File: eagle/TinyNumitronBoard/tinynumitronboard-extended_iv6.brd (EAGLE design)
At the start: 100 x 50 mm, 42 parts

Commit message: Last changes but problem with drill holes
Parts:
- removed U$3: (no value), kalshagar-images:GEARS_1000X500
- added U$1: (no value), kalshagar-images:SNOW1_1000X500
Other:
- board text added: "DATA (in)"
- board text added: "DATA (out)"
- board text removed: "DATA(in)"
- board text removed: "DATA(out)"
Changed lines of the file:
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@@
 <layer number="207" name="207bmp" color="8" fill="10" visible="no" active="yes"/>
 <layer number="208" name="208bmp" color="9" fill="10" visible="no" active="yes"/>
-<layer number="209" name="209bmp" color="7" fill="1" visible="no" active="yes"/>
+<layer number="209" name="209bmp" color="7" fill="1" visible="yes" active="yes"/>
 <layer number="210" name="210bmp" color="7" fill="1" visible="no" active="yes"/>
 <layer number="211" name="211bmp" color="7" fill="1" visible="no" active="yes"/>
@@
 <text x="8.89" y="19.685" size="1.27" layer="52" font="vector" rot="MR0">LTCH</text>
 <text x="96.2025" y="19.685" size="1.27" layer="52" font="vector" rot="MR0">LTCH</text>
-<text x="12.065" y="24.765" size="1.27" layer="52" font="vector" rot="MR0">DATA(in)</text>
+<text x="8.493125" y="22.780625" size="1.27" layer="52" font="vector" rot="MR0">DATA
+(in)</text>
 <wire x1="1.27" y1="21.59" x2="3.81" y2="21.59" width="0.4064" layer="52"/>
 <wire x1="3.81" y1="21.59" x2="3.81" y2="26.67" width="0.4064" layer="52"/>
@@
 <wire x1="99.06" y1="21.59" x2="96.52" y2="21.59" width="0.4064" layer="52"/>
 <wire x1="96.52" y1="21.59" x2="96.52" y2="26.67" width="0.4064" layer="52"/>
-<text x="95.885" y="24.765" size="1.27" layer="52" font="vector" rot="MR0">DATA(out)</text>
+<text x="96.123125" y="23.1775" size="1.27" layer="52" font="vector" rot="MR0">DATA
+(out)</text>
 <text x="76.2" y="48.26" size="1.27" layer="52" font="vector" rot="MR0">http://electrogeek.cc/Alan numitron clock.html</text>
-<wire x1="76.2" y1="30.48" x2="72.39" y2="36.83" width="0.6096" layer="52"/>
-<wire x1="72.39" y1="36.83" x2="72.39" y2="30.48" width="0.6096" layer="52"/>
-<wire x1="72.39" y1="30.48" x2="72.39" y2="24.13" width="0.6096" layer="52"/>
-<wire x1="72.39" y1="24.13" x2="68.58" y2="30.48" width="0.6096" layer="52"/>
-<wire x1="72.39" y1="30.48" x2="74.93" y2="30.48" width="0.6096" layer="52"/>
+<wire x1="78.74" y1="27.94" x2="74.93" y2="34.29" width="0.6096" layer="52"/>
+<wire x1="74.93" y1="34.29" x2="74.93" y2="29.21" width="0.6096" layer="52"/>
+<wire x1="74.93" y1="29.21" x2="74.93" y2="22.86" width="0.6096" layer="52"/>
+<wire x1="74.93" y1="22.86" x2="71.12" y2="29.21" width="0.6096" layer="52"/>
+<wire x1="74.93" y1="29.21" x2="77.47" y2="29.21" width="0.6096" layer="52"/>
 <text x="70.1675" y="0.635" size="1.27" layer="52" font="vector" rot="MR0">Alan numitron clock - IV6 (v1.0 - Dec 2016)</text>
 <text x="0.635" y="28.575" size="1.4224" layer="52" font="vector" rot="MR180">[IN]</text>
@@
 <element name="H2" library="holes" package="2,8" value="MOUNT-HOLE2.8" x="96.52" y="46.0375"/>
 <element name="H3" library="holes" package="2,8" value="MOUNT-HOLE2.8" x="96.52" y="3.81" locked="yes"/>
-<element name="U$3" library="kalshagar-images" package="GEARS_1000X500" value="" x="1.5875" y="0.635"/>
 <element name="TUBE1" library="kalshagar" package="IV6_NUMITRON_PAC_LARGE" value="IV6_NUMITRONLARGE" x="15" y="25"/>
 <element name="DRIVER1" library="uln2803" package="SO18L" value="ULN2803" x="15.24" y="39.37" rot="MR180"/>
@@
 <element name="JP_DOT_TUBE1" library="SparkFun-Passives" package="PAD-JUMPER-2-NO_YES_SILK" value="JUMPER-PAD-2-NOYES_SILK" x="24.13" y="29.21" rot="MR270"/>
 <element name="JP_DOT_TUBE4" library="SparkFun-Passives" package="PAD-JUMPER-2-NO_YES_SILK" value="JUMPER-PAD-2-NOYES_SILK" x="76.2" y="16.51" rot="MR90"/>
+<element name="U$1" library="kalshagar-images" package="SNOW1_1000X500" value="" x="0" y="0"/>
 </elements>
 <signals>

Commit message: Crapped up, now fixing
Started version 2, ripped up everything
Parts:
- removed DRIVER2: ULN2803, uln2803:SO18L
- removed TP1, TP2, TP3, TP4: TPB2,54, testpad:B2,54
- added IC1: IC_TD62783-SO-18W, dp_devices:SO-18L
- JP_INPUT, JP_OUTPUT: device SparkFun:1X06 -> SparkFun-Connectors:1X05_NO_SILK
- moved JP_INPUT 2.54 mm to (2.54, 15.2)
- moved JP_OUTPUT 2.54 mm to (97.8, 15.2)
- moved J_LED_IN 2.54 mm to (2.54, 12.7)
- moved J_LED_OUT 2.54 mm to (97.8, 12.7)
- moved J_TUBEPOWER_IN 2.54 mm to (2.54, 27.9)
- moved J_TUBEPOWER_OUT 2.54 mm to (97.8, 27.9)
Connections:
- removed net DIODE: DRIVER1.10, DRIVER2.10, DRIVER3.10, DRIVER4.10, TP1.TP, TP2.TP, TP3.TP, TP4.TP
- net GND: now also IC1.9; no longer DRIVER2.9
- net GRID_P: now also IC1.10
- net N$14: now also IC1.17; no longer DRIVER2.18
- net N$16: now also IC1.18; no longer DRIVER2.17
- net N$17: now also IC1.16; no longer DRIVER2.16
- net N$21: no longer JP_OUTPUT.6
- net N$39: now also IC1.15; no longer DRIVER2.15
- net N$40: now also IC1.14; no longer DRIVER2.14
- net N$41: now also IC1.13; no longer DRIVER2.13
- net N$42: now also IC1.12; no longer DRIVER2.12
- net N$43: now also IC1.11; no longer DRIVER2.11
- net N$44: now also IC1.1; no longer DRIVER2.1
- net N$45: now also IC1.2; no longer DRIVER2.2
- net N$46: now also IC1.3; no longer DRIVER2.3
- net N$47: now also IC1.4; no longer DRIVER2.4
- net N$48: now also IC1.5; no longer DRIVER2.5
- net N$49: now also IC1.6; no longer DRIVER2.6
- net N$50: now also IC1.7; no longer DRIVER2.7
- net N$51: now also IC1.8; no longer DRIVER2.8
- net SER: no longer JP_INPUT.6
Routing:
- net VCC: track 258.2 -> 0.00 mm, vias 5 -> 0
- net FIL_M: track 204.9 -> 0.00 mm
- net RCK: track 202.9 -> 0.00 mm, vias 4 -> 0
- net SCK: track 188.5 -> 0.00 mm, vias 6 -> 0
- net N$13: track 154.2 -> 0.00 mm, vias 2 -> 0
- net FIL_P: track 133.1 -> 0.00 mm
- net GRID_P: track 117.2 -> 0.00 mm, vias 3 -> 0
- net N$23: track 47.9 -> 0.00 mm, vias 2 -> 0
- net N$21: track 46.2 -> 0.00 mm, vias 1 -> 0
- net N$65: track 39.8 -> 0.00 mm
- net N$53: track 39.8 -> 0.00 mm, vias 2 -> 0
- net SER: track 38.5 -> 0.00 mm, vias 1 -> 0
- net N$10: track 36.4 -> 0.00 mm, vias 2 -> 0
- net N$32: track 31.3 -> 0.00 mm
- net N$30: track 30.4 -> 0.00 mm
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- removed copper zone on layer 16, net GND
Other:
- board text added: "Alan numitron clock - IV6 (v2.0 - Jan 2017)"
- board text added: "DATA"
- board text added: "TD62783"
- board text added: "http://electrogeek.cc/Alan numitron clock iv6.html"
- board text removed: "Alan numitron clock - IV6 (v1.0 - Dec 2016)"
- board text removed: "DATA (in)"
- board text removed: "DATA (out)"
- board text removed: "http://electrogeek.cc/Alan numitron clock.html"

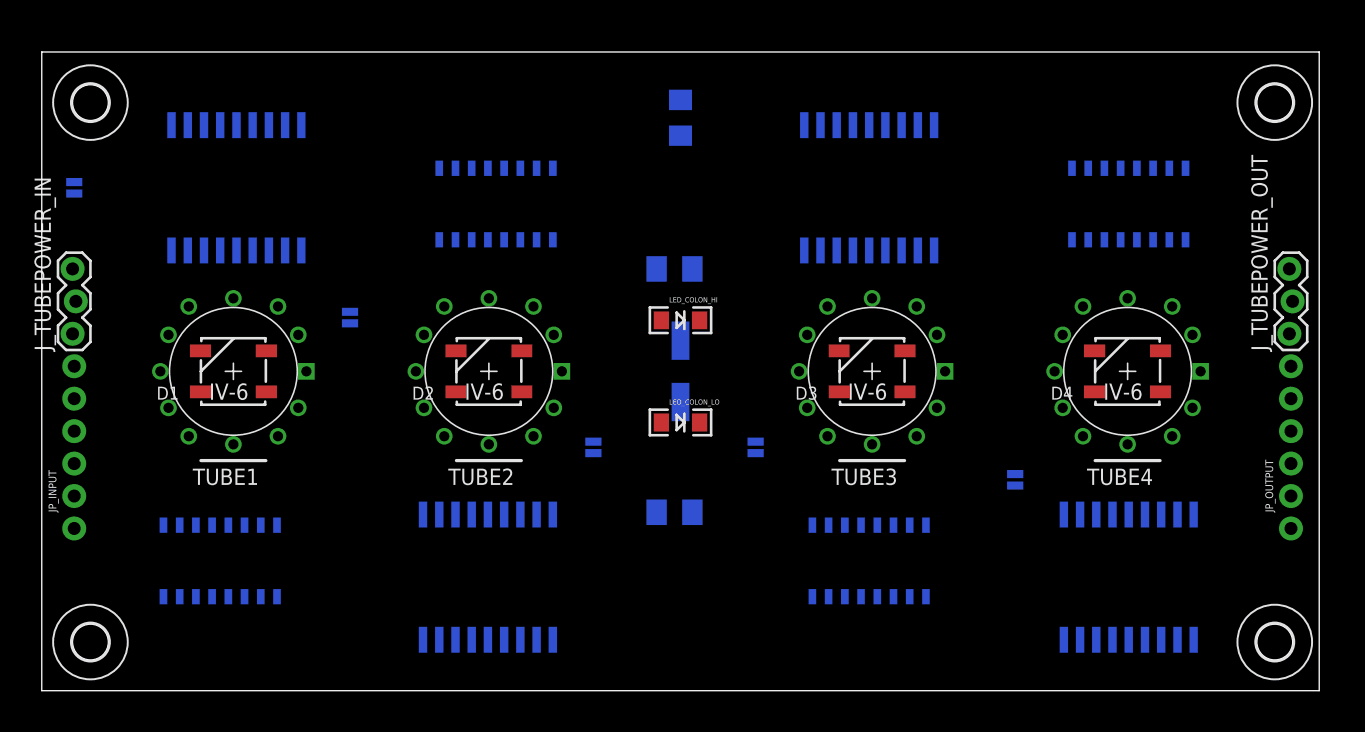
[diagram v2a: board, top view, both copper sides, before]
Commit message: Schematic fixed, placement done
Need to do routing now
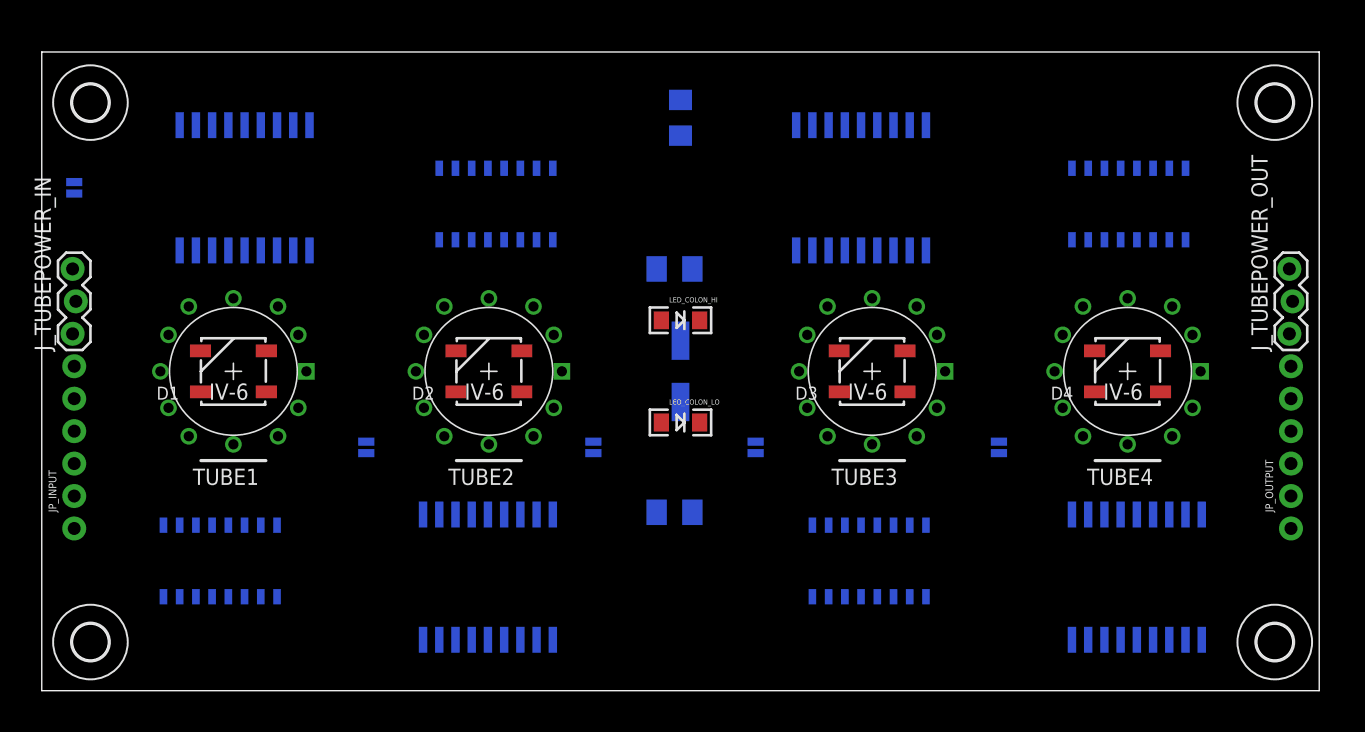
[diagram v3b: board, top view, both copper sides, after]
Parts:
- removed DRIVER1, DRIVER3, DRIVER4: ULN2803, uln2803:SO18L
- added PNPARRAY1, PNPARRAY3, PNPARRAY4: IC_TD62783-SO-18W, dp_devices:SO-18L
- moved JP_DOT_TUBE1 10.2 mm to (25.4, 19.1)
- moved JP_DOT_TUBE4 2.84 mm to (74.9, 19.1)
- renumbered IC1 to PNPARRAY2
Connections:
- net GND: now also PNPARRAY1.9, PNPARRAY3.9, PNPARRAY4.9; no longer DRIVER1.9, DRIVER3.9, DRIVER4.9
- net GRID_P: now also PNPARRAY1.10, PNPARRAY3.10, PNPARRAY4.10
- net N$1: now also PNPARRAY1.5, SER1.4; no longer DRIVER1.1, SER1.15
- net N$14: now also PNPARRAY2.18; no longer PNPARRAY2.17
- net N$15: now also PNPARRAY1.18; no longer DRIVER1.18
- net N$16: now also PNPARRAY2.17; no longer PNPARRAY2.18
- net N$18: now also PNPARRAY1.17; no longer DRIVER1.17
- net N$19: now also PNPARRAY1.16; no longer DRIVER1.16
- net N$2: now also PNPARRAY1.4, SER1.3; no longer DRIVER1.2, SER1.1
- net N$24: now also PNPARRAY4.18; no longer DRIVER4.18
- net N$25: now also PNPARRAY4.17; no longer DRIVER4.17
- net N$26: now also PNPARRAY4.16; no longer DRIVER4.16
- net N$27: now also PNPARRAY4.15; no longer DRIVER4.15
- net N$28: now also PNPARRAY4.14; no longer DRIVER4.14
- net N$29: now also PNPARRAY4.13; no longer DRIVER4.13
- net N$3: now also PNPARRAY1.3; no longer DRIVER1.3
- net N$30: now also PNPARRAY4.12; no longer DRIVER4.12
- net N$31: now also PNPARRAY4.11; no longer DRIVER4.11
- net N$32: now also PNPARRAY4.1; no longer DRIVER4.1
- net N$33: now also PNPARRAY4.2; no longer DRIVER4.2
- net N$34: now also PNPARRAY4.3; no longer DRIVER4.3
- net N$35: now also PNPARRAY4.4; no longer DRIVER4.4
- net N$36: now also PNPARRAY4.5; no longer DRIVER4.5
- net N$37: now also PNPARRAY4.6; no longer DRIVER4.6
- net N$38: now also PNPARRAY1.15; no longer DRIVER1.15
- net N$4: now also PNPARRAY1.2, SER1.1; no longer DRIVER1.4, SER1.3
- net N$5: now also PNPARRAY1.1, SER1.15; no longer DRIVER1.5, SER1.4
- net N$52: now also PNPARRAY4.7; no longer DRIVER4.7
- net N$54: now also PNPARRAY3.18; no longer DRIVER3.18
- net N$55: now also PNPARRAY1.14; no longer DRIVER1.14
- net N$56: now also PNPARRAY1.13; no longer DRIVER1.13
- net N$57: now also PNPARRAY1.12; no longer DRIVER1.12
- net N$58: now also PNPARRAY3.17; no longer DRIVER3.17
- net N$59: now also PNPARRAY1.11; no longer DRIVER1.11
- net N$6: now also PNPARRAY1.6; no longer DRIVER1.6
- net N$60: now also PNPARRAY3.16; no longer DRIVER3.16
- net N$61: now also PNPARRAY3.15; no longer DRIVER3.15
- net N$62: now also PNPARRAY3.14; no longer DRIVER3.14
- net N$63: now also PNPARRAY3.13; no longer DRIVER3.13
- net N$64: now also PNPARRAY3.12; no longer DRIVER3.12
- net N$65: now also PNPARRAY3.11; no longer DRIVER3.11
- net N$66: now also PNPARRAY3.1; no longer DRIVER3.1
- net N$67: now also PNPARRAY3.2; no longer DRIVER3.2
- net N$68: now also PNPARRAY3.3; no longer DRIVER3.3
- net N$69: now also PNPARRAY3.4; no longer DRIVER3.4
- net N$7: now also PNPARRAY1.7; no longer DRIVER1.7
- net N$70: now also PNPARRAY3.5; no longer DRIVER3.5
- net N$71: now also PNPARRAY3.6; no longer DRIVER3.6
- net N$72: now also PNPARRAY3.7; no longer DRIVER3.7
- net N$73: now also PNPARRAY3.8; no longer DRIVER3.8
- net N$74: now also PNPARRAY4.8; no longer DRIVER4.8
- net N$8: now also PNPARRAY1.8; no longer DRIVER1.8
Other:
- board text removed: "UL2803 Diode"
- board text removed: "ULN28003"

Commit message: Manual wiring WiP (30%)
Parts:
- removed FILGND2GND: JUMPER-PAD-2-NOYES_SILK, SparkFun-Passives:PAD-JUMPER-2-NO_YES_SILK
- removed J_TUBEPOWER_IN, J_TUBEPOWER_OUT: (no value), SparkFun-Connectors:1X03_LOCK
- added J1, J2: (no value), SparkFun-Connectors:1X02_NO_SILK
- moved JP_DOT_TUBE1 20.4 mm to (24.1, 39.4)
- moved PNPARRAY1 3.57 mm to (15.2, 42.9)
- moved PNPARRAY4 2.54 mm to (86.4, 6.35)
- moved PNPARRAY3 2.54 mm to (63.5, 41.9)
- moved SER2 2.54 mm to (14.0, 12.7)
- moved SER4 1.27 mm to (64.8, 11.4)
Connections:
- removed net FIL_M: FILGND2GND.1, J_TUBEPOWER_IN.3, J_TUBEPOWER_OUT.3, TUBE1.FIL_M, TUBE2.FIL_M, TUBE3.FIL_M, TUBE4.FIL_M
- net FIL_P: now also J1.2, J2.2; no longer J_TUBEPOWER_IN.2, J_TUBEPOWER_OUT.2
- net GND: now also TUBE1.FIL_M, TUBE2.FIL_M, TUBE3.FIL_M, TUBE4.FIL_M; no longer FILGND2GND.2
- net GRID_P: now also J1.1, J2.1; no longer J_TUBEPOWER_IN.1, J_TUBEPOWER_OUT.1
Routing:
- net GND: track 0.00 -> 299.0 mm
- net VCC: track 0.00 -> 249.9 mm, vias 0 -> 2
- net N$142: track 0.00 -> 174.3 mm, vias 0 -> 8
- net RCK: track 0.00 -> 137.0 mm, vias 0 -> 3
- net GRID_P: track 0.00 -> 107.7 mm, vias 0 -> 6
- net SCK: track 0.00 -> 71.2 mm, vias 0 -> 1
- net N$137: track 0.00 -> 50.8 mm, vias 0 -> 4
- net N$124: track 0.00 -> 47.1 mm
- net SER: track 0.00 -> 44.8 mm, vias 0 -> 2
- net N$122: track 0.00 -> 44.1 mm
- net N$128: track 0.00 -> 35.6 mm
- net N$126: track 0.00 -> 34.4 mm
- net N$129: track 0.00 -> 34.4 mm
- net N$127: track 0.00 -> 34.4 mm
- net N$110: track 0.00 -> 28.0 mm
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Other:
- board text removed: "-Fil"
- board text removed: "-Fil=GND"
